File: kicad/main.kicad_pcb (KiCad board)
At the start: 2 copper layers, 190.5 x 97.2 mm, 63 parts, among them J1 Jack-DC, J10 RS232, J11 UART, J2 LCD_Conn, J3 Data, J4 PWR, J5 uSD, J6 VIA_B, J7 IO~{EN}_{[2..7]}, J8 Control, J9 Addr, P1 Mini-DIN-6, SW1 Step, SW2 Reset, U1 74HC00, U2 74HC00, U3 MAX232, X1 4 MHz, X2 1.8432 MHz

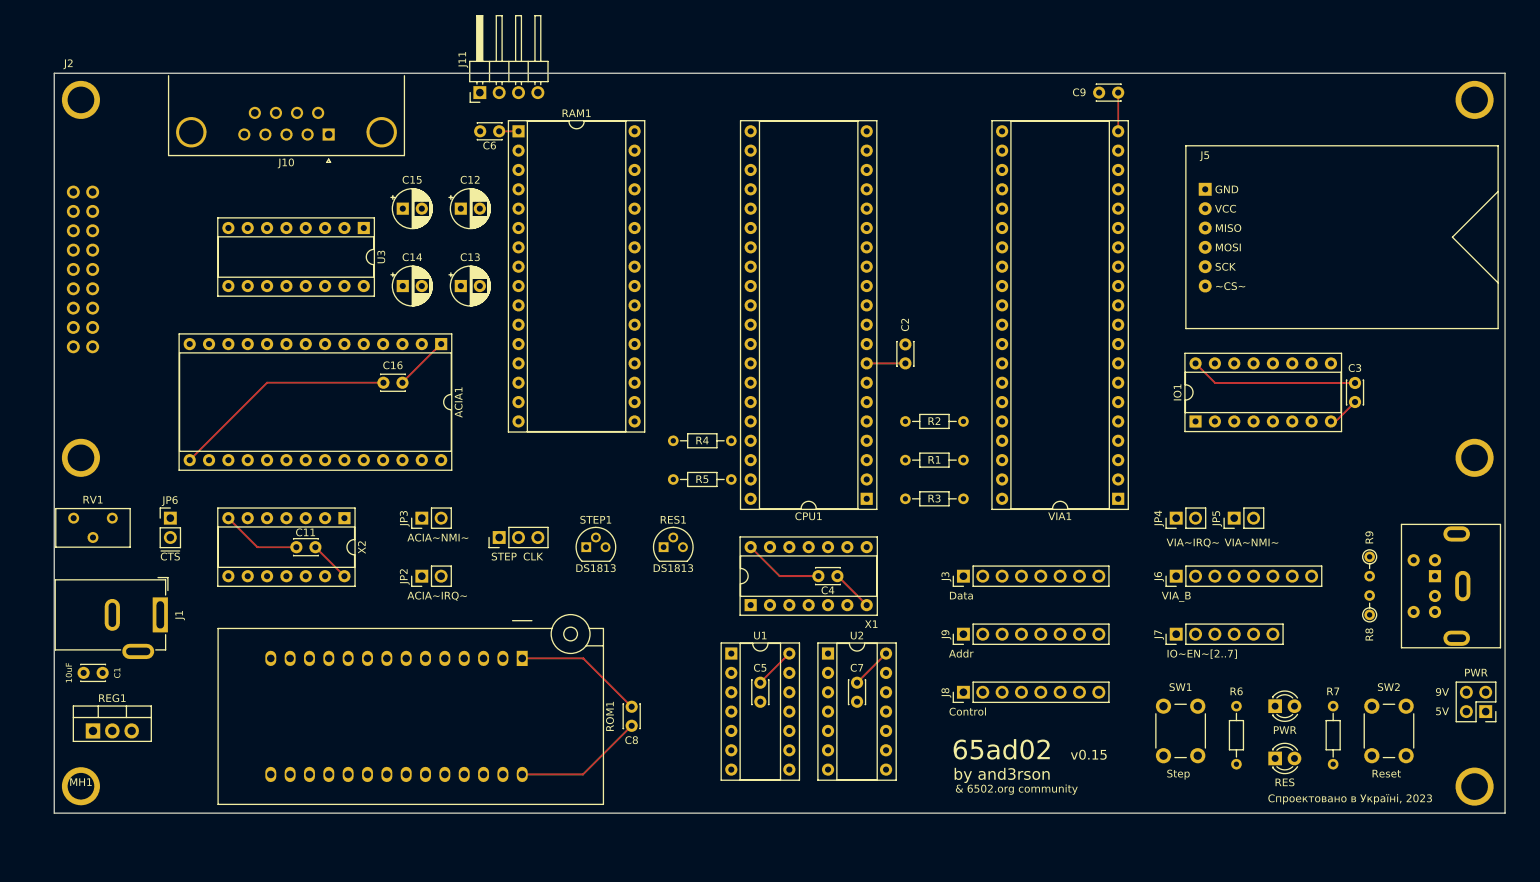
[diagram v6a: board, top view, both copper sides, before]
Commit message: Add RTC & CR2032 battery, increase size of decoupling capacitors
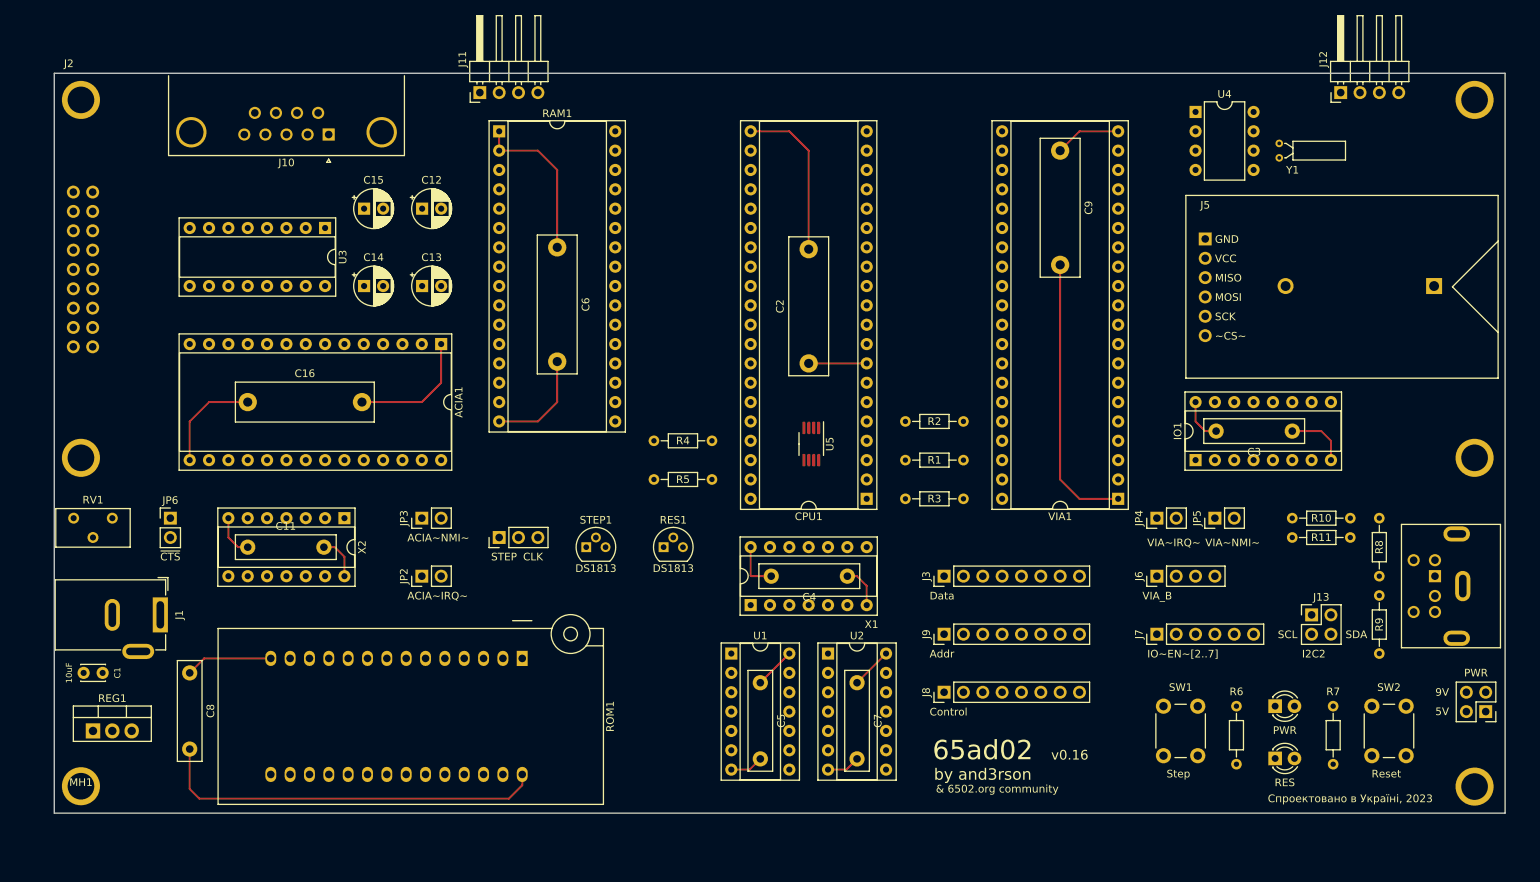
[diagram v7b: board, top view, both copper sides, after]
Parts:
- added BT1: CR2032, my:BatteryHolder_CR2032, B.Cu at (202.5, 45.7)
- added J12: I2C1, Connector_PinHeader_2.54mm:PinHeader_1x04_P2.54mm_Horizontal, F.Cu at (189.2, 20.3)
- added J13: I2C2, Connector_PinHeader_2.54mm:PinHeader_2x02_P2.54mm_Vertical, F.Cu at (185.4, 88.9)
- added R10: 5K, Resistor_THT:R_Axial_DIN0204_L3.6mm_D1.6mm_P7.62mm_Horizontal, F.Cu at (182.9, 76.2)
- added R11: 5K, Resistor_THT:R_Axial_DIN0204_L3.6mm_D1.6mm_P7.62mm_Horizontal, F.Cu at (182.9, 78.7)
- added U4: DS1307N+, Package_DIP:DIP-8_W7.62mm, F.Cu at (170.2, 22.9)
- added U5: MCP9808_MSOP, Package_SO:MSOP-8_3x3mm_P0.65mm, F.Cu at (119.7, 66.5)
- added Y1: 32.768 KHz, Crystal:Crystal_C26-LF_D2.1mm_L6.5mm_Horizontal, F.Cu at (181.2, 28.9)
- C11, C3, C4, C5, C7, C8: footprint Capacitor_THT:C_Disc_D3.0mm_W2.0mm_P2.50mm -> Capacitor_THT:C_Rect_L13.0mm_W3.0mm_P10.00mm_FKS3_FKP3_MKS4
- C16, C2, C6, C9: footprint Capacitor_THT:C_Disc_D3.0mm_W2.0mm_P2.50mm -> Capacitor_THT:C_Rect_L18.0mm_W5.0mm_P15.00mm_FKS3_FKP3
- J6: footprint Connector_PinHeader_2.54mm:PinHeader_1x08_P2.54mm_Vertical -> Connector_PinHeader_2.54mm:PinHeader_1x04_P2.54mm_Vertical
- R8, R9: footprint Resistor_THT:R_Axial_DIN0204_L3.6mm_D1.6mm_P2.54mm_Vertical -> Resistor_THT:R_Axial_DIN0204_L3.6mm_D1.6mm_P7.62mm_Horizontal
- moved C8 58.2 mm to (38.1, 96.5)
- moved C16 18.0 mm to (45.7, 61.0)
- moved C6 17.0 mm to (86.4, 40.6), turned to -90 degrees
- moved C2 12.7 mm to (119.4, 55.9)
- moved C9 10.8 mm to (152.4, 27.9), turned to -90 degrees
- moved C3 9.08 mm to (182.9, 64.8), turned to 180 degrees
- moved J5 6.52 mm to (168.9, 33.8)
- moved C11 6.39 mm to (45.7, 80.0)
- moved R8 5.24 mm to (194.3, 83.8)
- moved R9 5.24 mm to (194.3, 86.4)
- moved C12 5.08 mm to (68.6, 35.6)
- moved C13 5.08 mm to (68.6, 45.7)
- moved C14 5.08 mm to (61.0, 45.7)
- moved C15 5.08 mm to (61.0, 35.6)
- moved IO1 5.08 mm to (170.2, 68.6)
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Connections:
- VIA1 pad 15: Net-(J6-Pin_3) -> I^{2}CDATA
- VIA1 pad 16: Net-(J6-Pin_4) -> I^{2}CCLK
- VIA1 pad 17: Net-(J6-Pin_5) -> Net-(J6-Pin_3)
- VIA1 pad 18: Net-(J6-Pin_6) -> Net-(J6-Pin_4)
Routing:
- net GND: track 44.3 -> 128.5 mm
- net +5V: track 108.0 -> 131.8 mm
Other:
- board text added: "I2C2"
- board text added: "SCL"
- board text added: "SDA"
- board text added: "v0.16"
- board text removed: "v0.15"

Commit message: WIP: V16
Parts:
- removed C11, C4: 0,1uF, Capacitor_THT:C_Rect_L13.0mm_W3.0mm_P10.00mm_FKS3_FKP3_MKS4
- removed C14, C15: 10uF, Capacitor_THT:CP_Radial_D5.0mm_P2.50mm
- removed C5, C7: 0.1uF, Capacitor_THT:C_Rect_L13.0mm_W3.0mm_P10.00mm_FKS3_FKP3_MKS4
- removed J10: RS232, Connector_Dsub:DSUB-9_Male_Horizontal_P2.77x2.84mm_EdgePinOffset4.94mm_Housed_MountingHolesOffset7.48mm
- removed J11: UART, Connector_PinHeader_2.54mm:PinHeader_1x04_P2.54mm_Horizontal
- removed J13: I2C2, Connector_PinHeader_2.54mm:PinHeader_2x02_P2.54mm_Vertical
- removed JP1: Clock_Mode, Connector_PinHeader_2.54mm:PinHeader_1x03_P2.54mm_Vertical
- removed JP2: ACIA~{IRQ}, Connector_PinHeader_2.54mm:PinHeader_1x02_P2.54mm_Vertical
- removed JP3: ACIA~{NMI}, Connector_PinHeader_2.54mm:PinHeader_1x02_P2.54mm_Vertical
- removed JP4: VIA~{IRQ}, Connector_PinHeader_2.54mm:PinHeader_1x02_P2.54mm_Vertical
- removed JP5: VIA~{NMI}, Connector_PinHeader_2.54mm:PinHeader_1x02_P2.54mm_Vertical
- removed JP6: ~{CTS}, Connector_PinHeader_2.54mm:PinHeader_1x02_P2.54mm_Vertical
- removed STEP1: DS1813, Package_TO_SOT_THT:TO-92
- removed SW1: Step, Button_Switch_THT:SW_PUSH_6mm_H5mm
- added C10: 10uF, Capacitor_THT:C_Disc_D3.0mm_W2.0mm_P2.50mm, F.Cu at (199.4, 101.6)
- added D3: DATA, LED_THT:LED_D3.0mm, F.Cu at (208.3, 71.1)
- added J14: LCD_Conn, my:LCD24064, F.Cu at (17.0, 22.6)
- added J15: VIA_A, Connector_PinHeader_2.54mm:PinHeader_2x06_P2.54mm_Vertical, F.Cu at (200.7, 58.4)
- added MH3: MountingHole, my:Hole_3.5x5, F.Cu at (209.6, 26.7)
- added R12: 300, Resistor_THT:R_Axial_DIN0204_L3.6mm_D1.6mm_P7.62mm_Horizontal, F.Cu at (209.6, 92.7)
- added R13: 10K, Resistor_THT:R_Axial_DIN0204_L3.6mm_D1.6mm_P7.62mm_Horizontal, F.Cu at (201.9, 85.1)
- added R14: 10K, Resistor_THT:R_Axial_DIN0204_L3.6mm_D1.6mm_P7.62mm_Horizontal, F.Cu at (204.5, 85.1)
- added R15: 10K, Resistor_THT:R_Axial_DIN0204_L3.6mm_D1.6mm_P7.62mm_Horizontal, F.Cu at (207.0, 85.1)
- added SW3: SW_PWR, my:PB22E06, F.Cu at (16.5, 106.9)
- added U6: GAL16V8, Package_DIP:DIP-20_W7.62mm_Socket, F.Cu at (55.9, 88.9)
- added U7: ESP-01, my:ESP-01, F.Cu at (205.7, 77.5)
- C12: value 10uF -> 22uF; footprint Capacitor_THT:CP_Radial_D5.0mm_P2.50mm -> Capacitor_THT:C_Disc_D3.0mm_W2.0mm_P2.50mm
- C13: value 10uF -> 0.1uF; footprint Capacitor_THT:CP_Radial_D5.0mm_P2.50mm -> Capacitor_THT:C_Rect_L18.0mm_W5.0mm_P15.00mm_FKS3_FKP3
- J12: footprint Connector_PinHeader_2.54mm:PinHeader_1x04_P2.54mm_Horizontal -> Connector_PinHeader_2.54mm:PinHeader_2x02_P2.54mm_Vertical
- J2: value LCD_Conn -> UART; footprint my:LCD_4004 -> Connector_PinHeader_2.54mm:PinHeader_1x04_P2.54mm_Horizontal
- J7: value IO~{EN}_{[2..7]} -> IO~{EN}_{[3..7]}; footprint Connector_PinHeader_2.54mm:PinHeader_1x06_P2.54mm_Vertical -> Connector_PinHeader_2.54mm:PinHeader_1x05_P2.54mm_Vertical
- R8, R9: footprint Resistor_THT:R_Axial_DIN0204_L3.6mm_D1.6mm_P7.62mm_Horizontal -> Resistor_THT:R_Axial_DIN0204_L3.6mm_D1.6mm_P2.54mm_Vertical
- U3: value MAX232 -> AMS1117; footprint Package_DIP:DIP-16_W7.62mm_Socket -> Package_TO_SOT_SMD:SOT-223-3_TabPin2
- X1: value 4 MHz -> 16 MHz
- moved RV1 176.9 mm to (203.2, 52.1), turned to 180 degrees
- moved U3 161.7 mm to (205.7, 98.8), turned to 0 degrees
- moved C12 144.3 mm to (199.4, 96.5), turned to 90 degrees
- moved RES1 93.3 mm to (190.5, 104.1)
- moved R9 61.6 mm to (203.2, 25.4)
- moved R8 58.8 mm to (200.7, 25.4), turned to -90 degrees
- moved CPU1 56.4 mm to (94.0, 27.9), turned to 0 degrees
- moved VIA1 56.4 mm to (127.0, 27.9), turned to 0 degrees
- moved C9 49.1 mm to (134.6, 73.7), turned to 90 degrees
- moved P1 46.3 mm to (204.7, 37.7)
- moved BT1 43.5 mm to (161.3, 31.8), turned to -90 degrees
- moved J12 42.6 mm to (208.3, 58.4), turned to 0 degrees
- moved RAM1 40.7 mm to (76.2, 66.0), turned to 180 degrees
- moved C13 40.4 mm to (59.8, 85.1)
- moved U5 36.4 mm to (101.2, 35.1), turned to 90 degrees
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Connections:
- ACIA1 pad 10: Net-(ACIA1-TxD) -> TX
- ACIA1 pad 12: Net-(ACIA1-RxD) -> RX
- ACIA1 pad 26: Net-(ACIA1-~{IRQ}) -> ~{IRQ}
- ACIA1 pad 8: Net-(ACIA1-~{RTS}) -> unconnected-(ACIA1-~{RTS}-Pad8)
- ACIA1 pad 9: Net-(ACIA1-~{CTS}) -> GND
- C12 pad 1: Net-(U3-C2+) -> +3.3V
- C12 pad 2: Net-(U3-C2-) -> GND
- C13 pad 1: Net-(U3-C1+) -> +5V
- C13 pad 2: Net-(U3-C1-) -> GND
- CPU1 pad 37: Ф2 -> PHV
- IO1 pad 13: IO~{EN}_{2} -> LCD~{EN}
- J1 pad 1: +9V -> Net-(J1-Pad1)
- J1 pad 2: GND -> Net-(J1-Pad2)
- J2 pad 1: LCDD7 -> GND
- J2 pad 2: LCDD6 -> +5V
- J2 pad 3: LCDD5 -> TX
- J2 pad 4: LCDD4 -> RX
- J7 pad 1: IO~{EN}_{2} -> IO~{EN}_{3}
- J7 pad 2: IO~{EN}_{3} -> IO~{EN}_{4}
- J7 pad 3: IO~{EN}_{4} -> IO~{EN}_{5}
- J7 pad 4: IO~{EN}_{5} -> IO~{EN}_{6}
- J7 pad 5: IO~{EN}_{6} -> IO~{EN}_{7}
- RV1 pad 1: GND -> +5V
- RV1 pad 2: Net-(J2-Pin_12) -> Net-(J14-Pin_4)
- RV1 pad 3: +5V -> Net-(J14-Pin_20)
- U3 pad 1: Net-(U3-C1+) -> GND
- U3 pad 2: Net-(U3-VS+) -> +3.3V
- U3 pad 3: Net-(U3-C1-) -> +5V
- VIA1 pad 2: LCDD4 -> Net-(J15-Pin_3)
- VIA1 pad 21: Net-(JP4-B) -> ~{IRQ}
- VIA1 pad 3: LCDD5 -> Net-(J15-Pin_4)
- VIA1 pad 39: unconnected-(VIA1-CA2-Pad39) -> Net-(J15-Pin_12)
- VIA1 pad 4: LCDD6 -> Net-(J15-Pin_5)
- VIA1 pad 40: unconnected-(VIA1-CA1-Pad40) -> Net-(J15-Pin_11)
- VIA1 pad 5: LCDD7 -> Net-(J15-Pin_6)
- VIA1 pad 6: LCDEN1 -> Net-(J15-Pin_7)
- VIA1 pad 7: LCDEN2 -> Net-(J15-Pin_8)
- VIA1 pad 8: LCDR~{W} -> Net-(J15-Pin_9)
- VIA1 pad 9: LCDRS -> Net-(J15-Pin_10)
- X1 pad 8: CLK -> Net-(U6-I1/CLK)
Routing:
- net +5V: track 131.8 -> 108.0 mm
- net GND: track 128.5 -> 114.0 mm
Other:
- board size 190.5 x 97.2 mm -> 198.1 x 99.1 mm
- board text added: "I2C"
- board text added: "VIA_A"
- board text added: "by and3rson & 6502.org community"
- board text added: "Спроектовано і виготовлено в Україні, 2023"
- board text removed: "& 6502.org community"
- board text removed: "ACIA~IRQ~"
- board text removed: "ACIA~NMI~"
- board text removed: "I2C2"
- board text removed: "SCL"
- board text removed: "SDA"
- board text removed: "Step"
- board text removed: "VIA~IRQ~"
- board text removed: "VIA~NMI~"
- board text removed: "by and3rson"
- board text removed: "Спроектовано в Україні, 2023"
